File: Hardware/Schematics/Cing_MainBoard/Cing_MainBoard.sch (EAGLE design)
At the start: 93 parts, among them IC1 L293D, IC2 LM1117T3.3-V, IC3 FT232RL, Q1 16mhz, U2 BMP180, U3 MPU-6050MPU6050

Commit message: MainBoard Upgrade
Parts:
- removed SJ1: (no value), jumper:SJ
- added U$22: OPENSOURCE, Cing Library:OPENSOURCE
- added U$6: BATTERY_CONECTOR_D, Cing Library:BATTERY_CONECTOR_D
- IC2: value LM1117T3.3-V -> LM1117-3.3V
- U$2: value BIG_HEADER -> Header 2
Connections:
- removed net N$28: IRFU9024.S, REVERSE.C, SJ1.2, U$7.+, U$9.COM
- new net N$21: IRFU9024.S, REVERSE.C, U$9.COM
- net GND: now also U$6.-
- net IRFU: now also U$7.+; no longer SJ1.1
- net VCC_MOT: now also U$6.+
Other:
- moved on the sheet: U$7

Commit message: upgrading board
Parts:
- removed C6: 100uf, rcl:CPOL-EUE3.5-8
- added JP2: ServoA, pinhead:PINHD-1X3
- added JP3: ServoB, pinhead:PINHD-1X3
- added JP4: ServoC, pinhead:PINHD-1X3
- added R21, R23: PHOTOCELL1, LDR:PHOTOCELL1
- added R29, R32: 1k, rcl:R-EU_R1206
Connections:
- removed net HD_A7: U$1.A7, U$2.A7
- new net A7: R21.P$2, R32.1, U$1.A7, U$2.A7
- net +3V3: now also R29.2, R32.2; no longer C6.+
- net A6: now also R23.P$2, R29.1
- net D6: now also JP4.1
- net GND: now also JP2.3, JP3.3, JP4.3, R21.P$1, R23.P$1; no longer C6.-
- net IN_A1: now also JP3.1
- net IN_A2: now also JP2.1
- net VCC_MOT: now also JP2.2, JP3.2, JP4.2

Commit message: Final
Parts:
- added POT: 100k, pot:TRIM_EU-RJ9W
- added TSOP4838: TSOP4838, Cing Library:TSOP4838
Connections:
- net +3V3: now also POT.E, TSOP4838.V+
- net A1: now also POT.S
- net D4: now also TSOP4838.OUT
- net GND: now also POT.A, TSOP4838.GND
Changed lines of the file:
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@@
 <part name="JP4" library="pinhead" library_urn="urn:adsk.eagle:library:325" deviceset="PINHD-1X3" device="" package3d_urn="urn:adsk.eagle:package:22458/2" value="ServoC"/>
 <part name="GND43" library="supply1" library_urn="urn:adsk.eagle:library:371" deviceset="GND" device=""/>
+<part name="TSOP4838" library="Cing Library" deviceset="TSOP4838" device=""/>
+<part name="+3V22" library="supply1" library_urn="urn:adsk.eagle:library:371" deviceset="+3V3" device=""/>
+<part name="GND44" library="supply1" library_urn="urn:adsk.eagle:library:371" deviceset="GND" device=""/>
+<part name="POT" library="pot" library_urn="urn:adsk.eagle:library:331" deviceset="TRIM_EU-" device="RJ9W" package3d_urn="urn:adsk.eagle:package:22702/1" value="100k"/>
+<part name="+3V23" library="supply1" library_urn="urn:adsk.eagle:library:371" deviceset="+3V3" device=""/>
+<part name="GND45" library="supply1" library_urn="urn:adsk.eagle:library:371" deviceset="GND" device=""/>
 </parts>
 <sheets>
@@
 <instance part="+3V20" gate="G$1" x="35.56" y="175.26" rot="MR0"/>
 <instance part="+3V21" gate="G$1" x="35.56" y="149.86" rot="MR0"/>
+<instance part="TSOP4838" gate="G$1" x="119.38" y="35.56"/>
+<instance part="+3V22" gate="G$1" x="132.08" y="45.72"/>
+<instance part="GND44" gate="1" x="132.08" y="25.4" rot="MR0"/>
+<instance part="POT" gate="1" x="134.62" y="71.12"/>
+<instance part="+3V23" gate="G$1" x="134.62" y="81.28"/>
+<instance part="GND45" gate="1" x="134.62" y="60.96" rot="MR0"/>
 </instances>
 <busses>
@@
 <pinref part="GND40" gate="1" pin="GND"/>
 <wire x1="17.78" y1="154.94" x2="17.78" y2="160.02" width="0.1524" layer="91"/>
+</segment>
+<segment>
+<pinref part="TSOP4838" gate="G$1" pin="GND"/>
+<pinref part="GND44" gate="1" pin="GND"/>
+<wire x1="127" y1="30.48" x2="132.08" y2="30.48" width="0.1524" layer="91"/>
+<wire x1="132.08" y1="30.48" x2="132.08" y2="27.94" width="0.1524" layer="91"/>
+</segment>
+<segment>
+<pinref part="POT" gate="1" pin="A"/>
+<pinref part="GND45" gate="1" pin="GND"/>
+<wire x1="134.62" y1="63.5" x2="134.62" y2="66.04" width="0.1524" layer="91"/>
 </segment>
 </net>
@@
 <pinref part="+3V21" gate="G$1" pin="+3V3"/>
 </segment>
+<segment>
+<pinref part="TSOP4838" gate="G$1" pin="V+"/>
+<pinref part="+3V22" gate="G$1" pin="+3V3"/>
+<wire x1="127" y1="40.64" x2="132.08" y2="40.64" width="0.1524" layer="91"/>
+<wire x1="132.08" y1="40.64" x2="132.08" y2="43.18" width="0.1524" layer="91"/>
+</segment>
+<segment>
+<pinref part="POT" gate="1" pin="E"/>
+<pinref part="+3V23" gate="G$1" pin="+3V3"/>
+<wire x1="134.62" y1="78.74" x2="134.62" y2="76.2" width="0.1524" layer="91"/>
+</segment>
 </net>
 <net name="SCK" class="0">
@@
 </segment>
 </net>
+<net name="D4" class="0">
+<segment>
+<pinref part="TSOP4838" gate="G$1" pin="OUT"/>
+<wire x1="127" y1="35.56" x2="132.08" y2="35.56" width="0.1524" layer="91"/>
+<label x="132.08" y="35.56" size="1.778" layer="95" xref="yes"/>
+</segment>
+</net>
+<net name="A1" class="0">
+<segment>
+<pinref part="POT" gate="1" pin="S"/>
+<wire x1="139.7" y1="71.12" x2="142.24" y2="71.12" width="0.1524" layer="91"/>
+<label x="142.24" y="71.12" size="1.778" layer="95" xref="yes"/>
+</segment>
+</net>

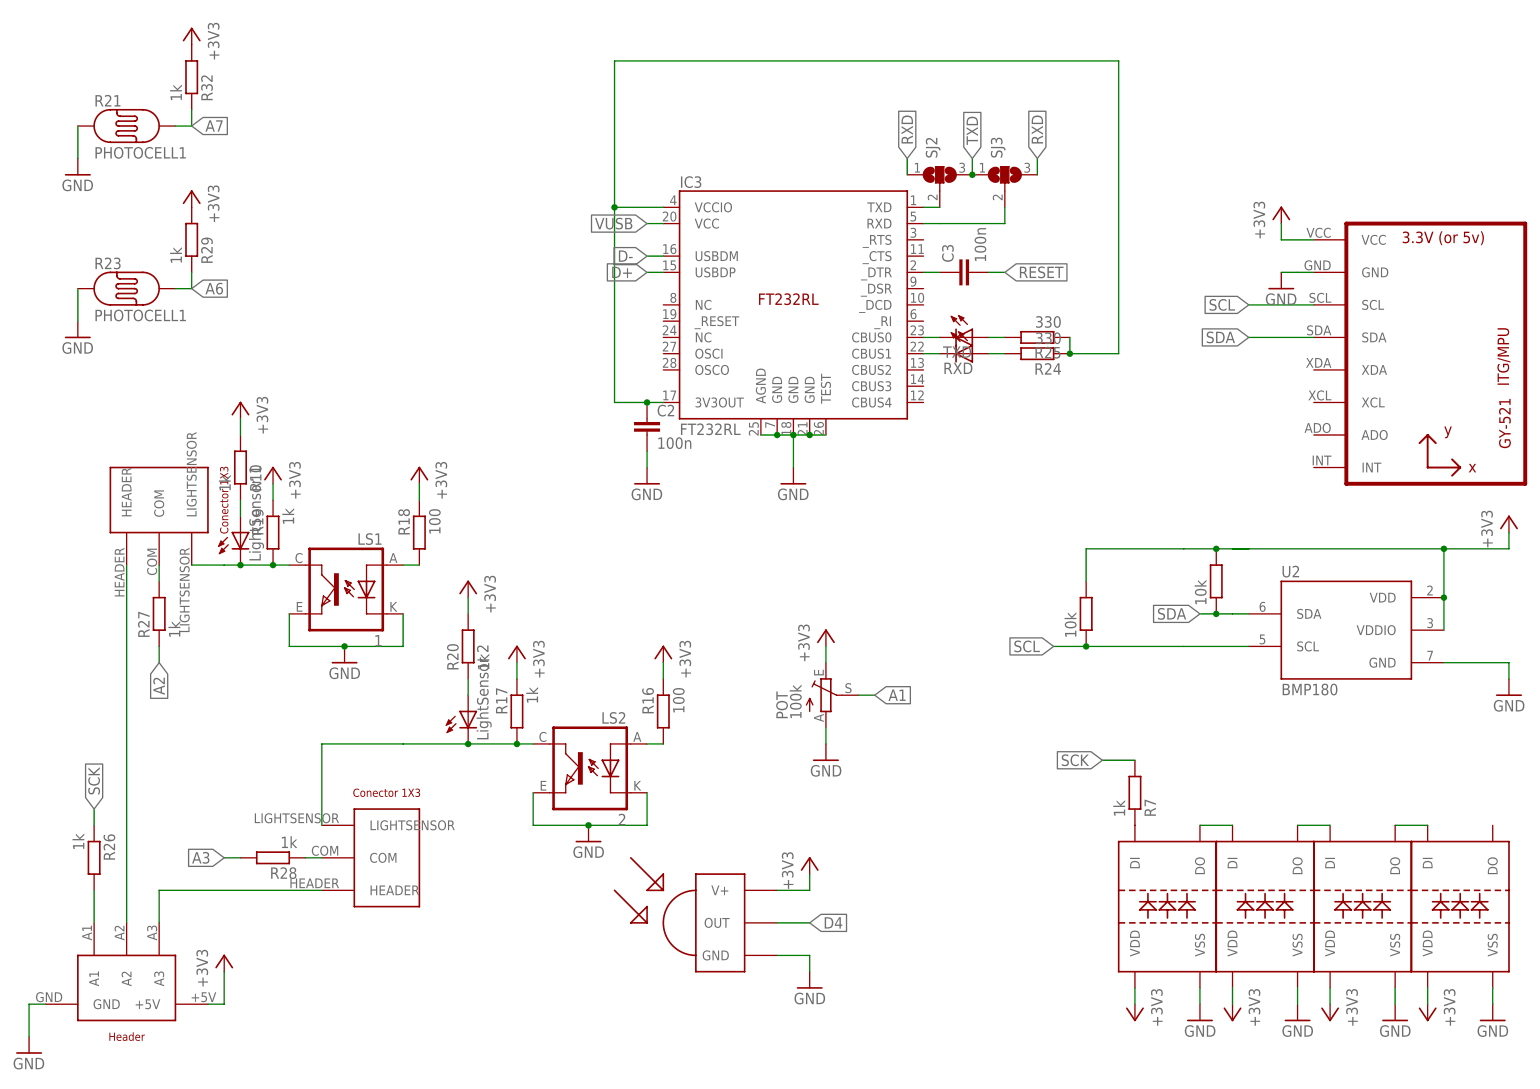
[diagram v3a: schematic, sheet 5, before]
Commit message: board change
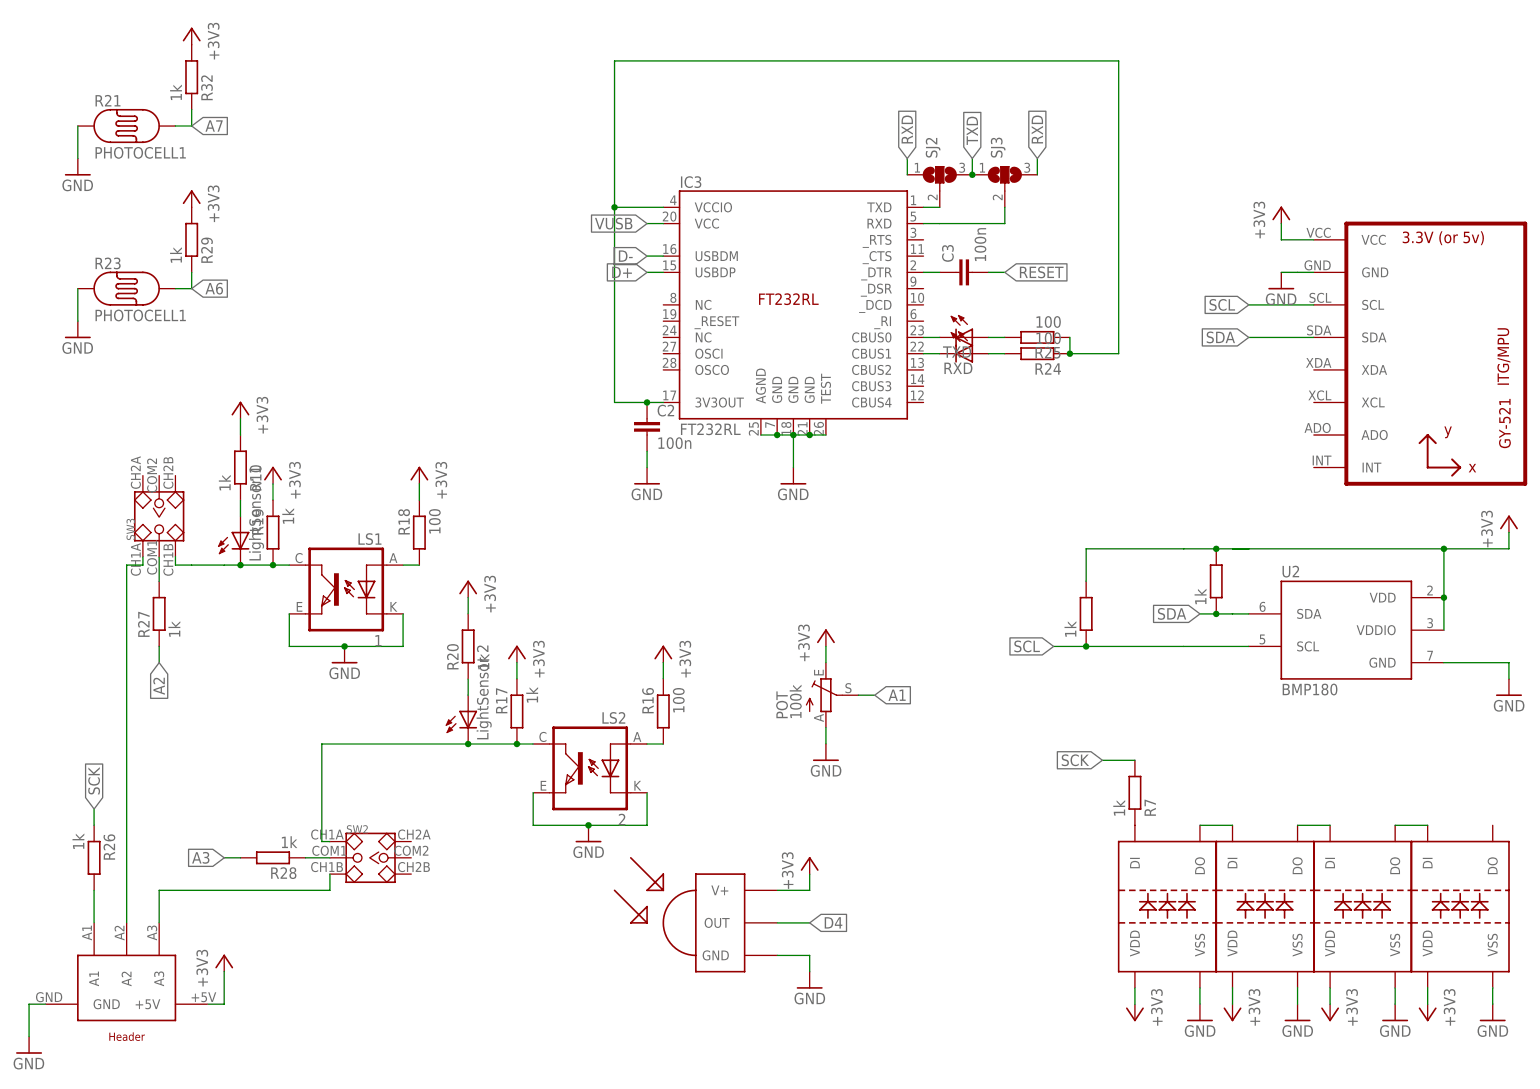
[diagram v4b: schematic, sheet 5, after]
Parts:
- removed U$13, U$14: CONNECTOR_LIGHT_SENSOR, Cing Library:CONNECTOR_LIGHT_SENSOR
- removed U$15: CONNECTOR_BUTTON, Cing Library:CONNECTOR_BUTTON
- added SW2, SW3, SW4: (no value), Cing Library:USB_SWITCH
- R1, R12, R13, R14, R15, R30, R31: value 10k -> 1k
- R22, R6: value 1k -> 100
- R24, R25: value 330 -> 100
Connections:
- net A6: now also SW4.COM1; no longer U$15.COM
- net BUTTON: now also SW4.CH1B; no longer U$15.BUTTON
- net HD_A6: now also SW4.CH1A; no longer U$15.HEADER
- net N$10: now also SW2.COM1; no longer U$14.COM
- net N$24: now also SW3.CH1B; no longer U$13.LIGHTSENSOR
- net N$31: now also SW3.CH1A; no longer U$13.HEADER
- net N$40: now also SW2.CH1B; no longer U$14.HEADER
- net N$43: now also SW3.COM1; no longer U$13.COM
- net N$45: now also SW2.CH1A; no longer U$14.LIGHTSENSOR
